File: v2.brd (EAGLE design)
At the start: 24 x 24 mm, 46 parts, among them Q1 12MHz

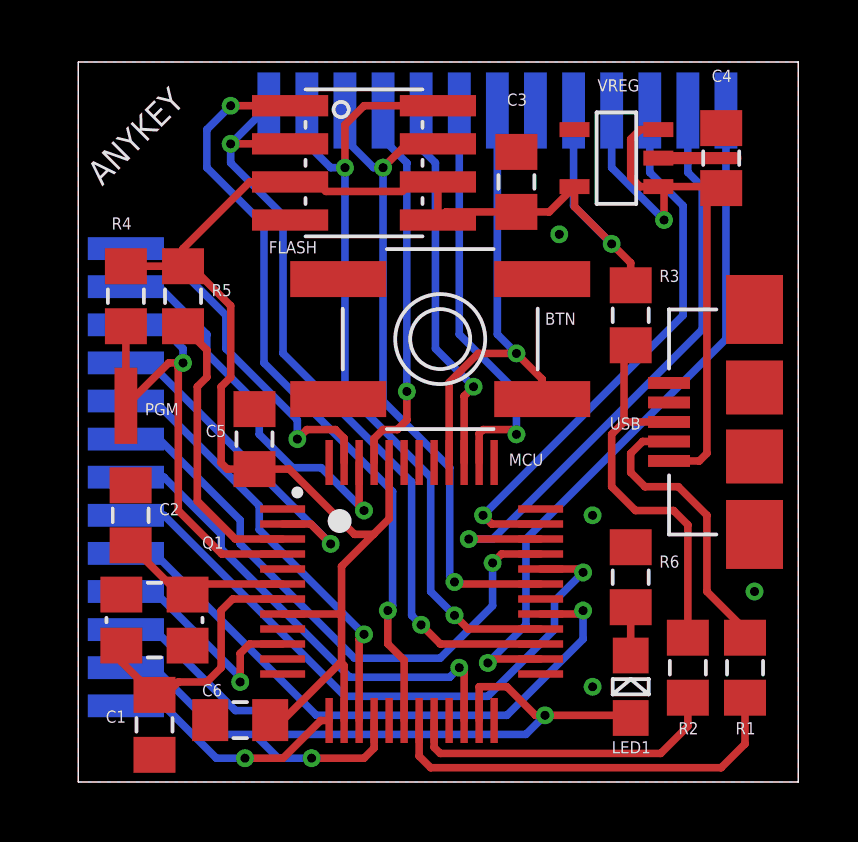
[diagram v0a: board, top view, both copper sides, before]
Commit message: Added drill hole, simplified routing, added version number on silkscreen, flash pinout fix, added softconnect transistor
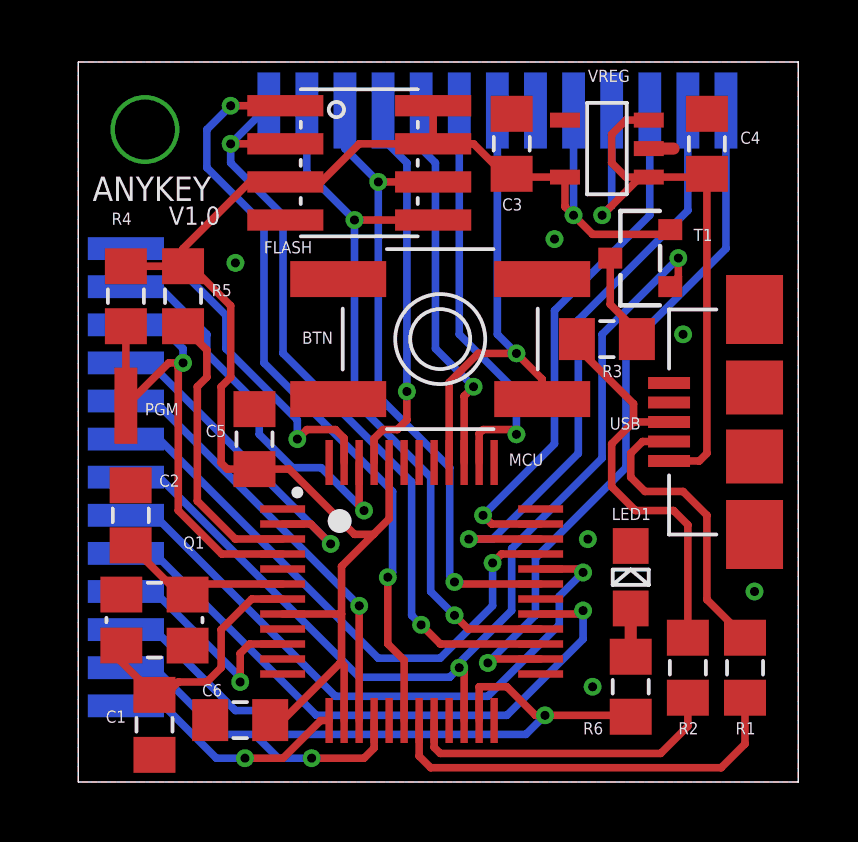
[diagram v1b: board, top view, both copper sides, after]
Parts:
- added T1: BSS84, MEINZEUG:SOT23
- JP21: value VPOWER -> PWR
- moved LED1 3.65 mm to (18.4, 6.83)
- moved R6 3.65 mm to (18.4, 3.17)
- moved C3 1.28 mm to (14.4, 21.3)
- moved R3 1.12 mm to (17.6, 14.8), turned to 180 degrees
- moved C4 0.67 mm to (21.0, 21.3)
- moved VREG 0.45 mm to (17.6, 21.1)
- moved FLASH 0.16 mm to (9.37, 20.6)
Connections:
- net N$4 renamed USB_DM
- net N$6 renamed USB_DP
- net USB_D- renamed N$4
- removed net PIO0_6: JP5.P$1, MCU.22
- new net !USB_CONNECT: JP5.P$1, MCU.22, T1.1
- new net N$3: R3.1, T1.3
- net GND: now also LED1.K; no longer R6.1
- net N$5: now also LED1.A, R6.1; no longer LED1.K, R6.2
- net PIO0_7: now also R6.2; no longer LED1.A
- net VD33: now also T1.2; no longer R3.1
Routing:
- net !USB_CONNECT: track 0.00 -> 33.8 mm, vias 0 -> 2
- net PIO0_6: track 16.1 -> 0.00 mm, vias 1 -> 0
- net N$3: track 0.00 -> 3.07 mm
- net MOSI: track 27.0 -> 24.5 mm
- net GND: track 2.57 -> 0.83 mm, vias 4 -> 7
- net USB_D+: track 13.3 -> 14.4 mm
- net PIO1_2: track 18.8 -> 17.8 mm
- net VD33: track 55.6 -> 55.0 mm
- net SCK: track 22.5 -> 22.0 mm
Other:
- board text added: "V1.0"

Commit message: Changed mounting hole to drill, adjustments to meet Makepcb.com design limitations (i.e. move oscillator), some more trace straightening
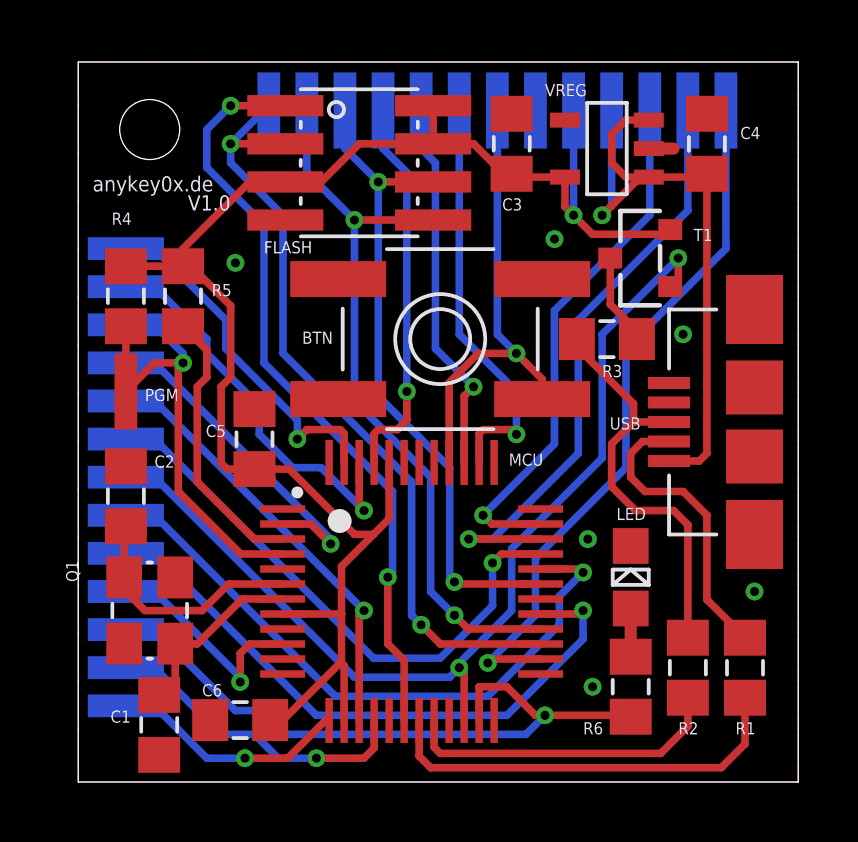
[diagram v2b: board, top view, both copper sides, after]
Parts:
- moved C2 0.65 mm to (1.59, 9.53)
- moved PGM 0.48 mm to (1.59, 13.0)
- moved Q1 0.35 mm to (2.38, 5.71), turned to 270 degrees
- moved C1 0.16 mm to (2.70, 1.91)
- renumbered LED1 to LED
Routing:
- net N$2: track 8.44 -> 6.19 mm
- net N$1: track 5.89 -> 8.08 mm
- net PIO0_1: track 16.9 -> 15.8 mm
- net GND: vias 7 -> 6
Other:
- board text added: "anykey0x.de"
- board text removed: "ANYKEY"

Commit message: Board adjustments to comply with MakePCB.com
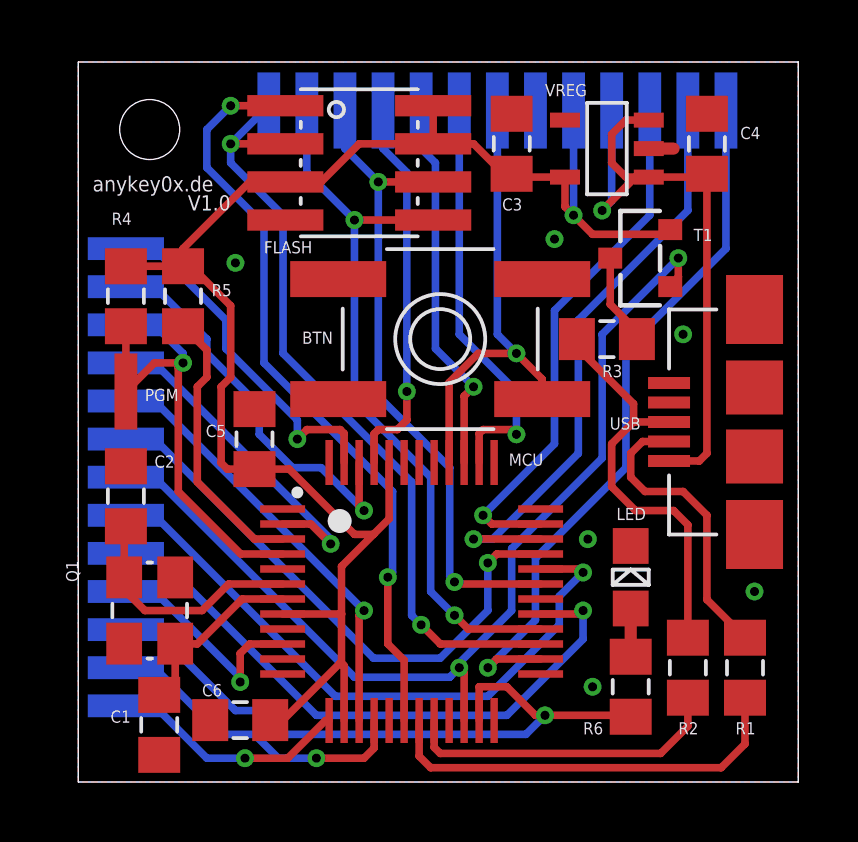
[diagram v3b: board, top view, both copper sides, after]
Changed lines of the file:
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@@
 </element>
 <element name="JP21" library="MEINZEUG" package="PCB_MEDIUM_RECT_PAD" value="PWR" x="17.78" y="22.38375" smashed="yes" rot="MR270">
-<attribute name="VALUE" x="17.93875" y="20.47875" size="0.4064" layer="22" font="vector" rot="MR270"/>
+<attribute name="VALUE" x="17.93875" y="20.6375" size="0.4064" layer="22" font="vector" rot="MR270"/>
 </element>
 <element name="JP22" library="MEINZEUG" package="PCB_MEDIUM_RECT_PAD" value="GND" x="15.24" y="22.38375" smashed="yes" rot="MR270">
@@
 <contactref element="VREG" pad="2"/>
 <contactref element="BTN" pad="A"/>
-<polygon width="0.254" layer="1">
+<polygon width="0.254" layer="1" isolate="0.0508">
 <vertex x="0" y="0"/>
 <vertex x="0" y="24"/>
@@
 <contactref element="FLASH" pad="4"/>
 <contactref element="JP22" pad="P$1"/>
-<polygon width="0.254" layer="16">
+<polygon width="0.254" layer="16" isolate="0.0508">
 <vertex x="0" y="0"/>
 <vertex x="24" y="0"/>
@@
 <contactref element="MCU" pad="34"/>
 <contactref element="JP13" pad="P$1"/>
-<via x="13.0175" y="8.09625" extent="1-16" drill="0.3"/>
-<wire x1="13.81125" y1="8.09625" x2="13.0175" y2="8.09625" width="0.254" layer="16"/>
-<wire x1="15.4125" y1="8.1" x2="13.02125" y2="8.1" width="0.254" layer="1"/>
-<wire x1="13.02125" y1="8.1" x2="13.0175" y2="8.09625" width="0.254" layer="1"/>
+<via x="13.17625" y="8.09625" extent="1-16" drill="0.3"/>
+<wire x1="13.81125" y1="8.09625" x2="13.17625" y2="8.09625" width="0.254" layer="16"/>
+<wire x1="15.4125" y1="8.1" x2="13.18" y2="8.1" width="0.254" layer="1"/>
+<wire x1="13.18" y1="8.1" x2="13.17625" y2="8.09625" width="0.254" layer="1"/>
 <wire x1="13.81125" y1="8.09625" x2="16.66875" y2="10.95375" width="0.254" layer="16"/>
 <wire x1="16.66875" y1="10.95375" x2="16.66875" y2="15.39875" width="0.254" layer="16"/>
@@
 <contactref element="JP12" pad="P$1"/>
 <contactref element="MCU" pad="33"/>
-<wire x1="15.4125" y1="7.6" x2="14.10875" y2="7.6" width="0.254" layer="1"/>
-<wire x1="14.10875" y1="7.6" x2="13.81125" y2="7.3025" width="0.254" layer="1"/>
-<via x="13.81125" y="7.3025" extent="1-16" drill="0.3"/>
+<wire x1="15.4125" y1="7.6" x2="13.95" y2="7.6" width="0.254" layer="1"/>
+<wire x1="13.95" y1="7.6" x2="13.6525" y2="7.3025" width="0.254" layer="1"/>
+<via x="13.6525" y="7.3025" extent="1-16" drill="0.3"/>
 <wire x1="9.8425" y1="4.1275" x2="12.065" y2="4.1275" width="0.254" layer="16"/>
-<wire x1="13.81125" y1="5.87375" x2="13.81125" y2="7.3025" width="0.254" layer="16"/>
+<wire x1="13.6525" y1="5.715" x2="13.6525" y2="7.3025" width="0.254" layer="16"/>
 <wire x1="9.8425" y1="4.1275" x2="2.54" y2="11.43" width="0.254" layer="16"/>
 <wire x1="1.5875" y1="11.43" x2="2.54" y2="11.43" width="0.254" layer="16"/>
-<wire x1="12.065" y1="4.1275" x2="13.81125" y2="5.87375" width="0.254" layer="16"/>
+<wire x1="12.065" y1="4.1275" x2="13.6525" y2="5.715" width="0.254" layer="16"/>
 </signal>
 <signal name="PIO0_11">
@@
 <contactref element="C4" pad="1"/>
 <wire x1="20.955" y1="10.95375" x2="20.70275" y2="10.7015" width="0.254" layer="1"/>
-<via x="17.4625" y="18.89125" extent="1-16" drill="0.3"/>
+<via x="17.4625" y="19.05" extent="1-16" drill="0.3"/>
 <contactref element="VREG" pad="3"/>
 <wire x1="20.955" y1="10.95375" x2="20.955" y2="20.2725" width="0.254" layer="1"/>
-<wire x1="19.01825" y1="20.163790625" x2="18.735040625" y2="20.163790625" width="0.254" layer="1"/>
-<wire x1="18.735040625" y1="20.163790625" x2="17.4625" y2="18.89125" width="0.254" layer="1"/>
+<wire x1="19.01825" y1="20.163790625" x2="18.576290625" y2="20.163790625" width="0.254" layer="1"/>
+<wire x1="18.576290625" y1="20.163790625" x2="17.4625" y2="19.05" width="0.254" layer="1"/>
 <contactref element="JP21" pad="P$1"/>
-<wire x1="17.78" y1="22.38375" x2="17.78" y2="19.20875" width="0.254" layer="16"/>
-<wire x1="17.78" y1="19.20875" x2="17.4625" y2="18.89125" width="0.254" layer="16"/>
+<wire x1="17.78" y1="22.38375" x2="17.78" y2="19.3675" width="0.254" layer="16"/>
+<wire x1="17.78" y1="19.3675" x2="17.4625" y2="19.05" width="0.254" layer="16"/>
 <wire x1="19.01825" y1="22.063709375" x2="18.253709375" y2="22.063709375" width="0.254" layer="1"/>
 <wire x1="18.253709375" y1="22.063709375" x2="17.78" y2="21.59" width="0.254" layer="1"/>
-<wire x1="18.735040625" y1="20.163790625" x2="18.253709375" y2="20.163790625" width="0.254" layer="1"/>
+<wire x1="18.576290625" y1="20.163790625" x2="18.253709375" y2="20.163790625" width="0.254" layer="1"/>
 <wire x1="18.253709375" y1="20.163790625" x2="17.78" y2="20.6375" width="0.254" layer="1"/>
 <wire x1="17.78" y1="20.6375" x2="17.78" y2="21.59" width="0.254" layer="1"/>
@@
 <contactref element="MCU" pad="26"/>
 <contactref element="JP25" pad="P$1"/>
-<wire x1="15.4125" y1="4.1" x2="13.78375" y2="4.1" width="0.254" layer="1"/>
-<wire x1="13.78375" y1="4.1" x2="13.6525" y2="3.96875" width="0.254" layer="1"/>
-<via x="13.6525" y="3.96875" extent="1-16" drill="0.3"/>
-<wire x1="15.24" y1="7.46125" x2="15.24" y2="5.55625" width="0.254" layer="16"/>
-<wire x1="15.24" y1="5.55625" x2="13.6525" y2="3.96875" width="0.254" layer="16"/>
+<wire x1="15.4125" y1="4.1" x2="13.9425" y2="4.1" width="0.254" layer="1"/>
+<wire x1="13.9425" y1="4.1" x2="13.6525" y2="3.81" width="0.254" layer="1"/>
+<via x="13.6525" y="3.81" extent="1-16" drill="0.3"/>
+<wire x1="15.24" y1="7.46125" x2="15.24" y2="5.3975" width="0.254" layer="16"/>
+<wire x1="15.24" y1="5.3975" x2="13.6525" y2="3.81" width="0.254" layer="16"/>
 <wire x1="21.59" y1="22.38375" x2="21.59" y2="17.78" width="0.254" layer="16"/>
 <wire x1="21.59" y1="17.78" x2="18.25625" y2="14.44625" width="0.254" layer="16"/>
